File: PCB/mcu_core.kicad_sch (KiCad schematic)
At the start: 11 parts

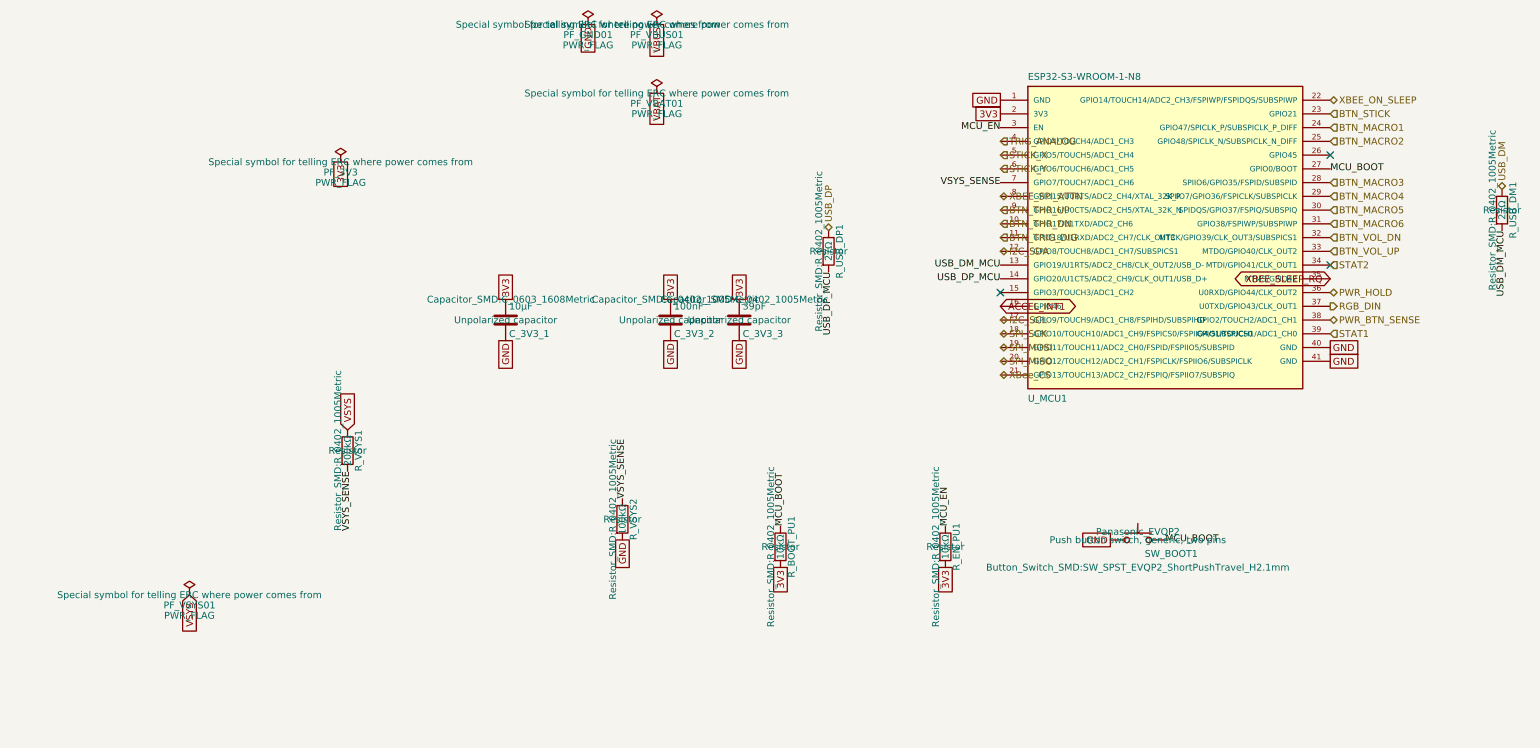
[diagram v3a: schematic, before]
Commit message: fix: make every BOM Value unambiguous for the fab, and switch D_INV_ISO1 to SOT-323 (#61)
* fix: make every BOM Value unambiguous for the fab, and switch D_INV_ISO1 to SOT-323

PCBWay flagged D_INV_ISO1: "BAT54W" is SOT-323 from nearly every maker, but we
had picked Yangjie's SOD-123 variant. A fab only sees Designator, Footprint,
Quantity and Value in the BOM (never MF/MPN/LCSC), so a bare part name is
ambiguous. Fixes the class of problem, not just this part:

- Every component's Value is now "<label> | <MPN> | <manufacturer> | <package>"
  (label dropped when it repeats the MPN; commas/periods stripped so the CSV
  never needs quoting). BT1 keeps its RIGHT-ANGLE HORIZONTAL note. Applied to
  all 81 parts across every sheet and the PCB.
- scripts/bom_values.py builds, applies, and checks these values, including
  that the PCB copy of Value/MF/MPN/footprint matches the schematic. New
  footprints must be added to its package table on purpose; hand-sourced parts
  with no MPN (J_STICK1) are listed explicitly.
- D_INV_ISO1 -> Diodes BAT54W-7-F in SOT-323 (common part, several makers).
  Pin 1 anode / pin 2 not connected / pin 3 cathode, confirmed against
  Nexperia's numbered pinning table and Diodes' datasheet. Uses KiCad's
  Diode:BAT54W symbol; PCB footprint replaced and rerouted. Electrically the
  same BAT54 family (30V, 200mA, 2uA leakage at 25V), so the SPICE model and
  scripts/spice/latch_sim.py still pass.
- Layout diagrams now say AO3401A for Q_PWR1 (they were stale since it was
  swapped from DMG2305UX) and BAT54W-7-F/SOT-323 for D_INV_ISO1.
- Repo CLAUDE.md documents the Value rule and the script.

ERC/DRC clean; production files regenerated.

Co-Authored-By: Claude Sonnet 5 <noreply@anthropic.com>

* chore: commit KiCad project settings (reordered used-designators list)

Co-Authored-By: Claude Sonnet 5 <noreply@anthropic.com>

---------

Co-authored-by: Claude Sonnet 5 <noreply@anthropic.com>
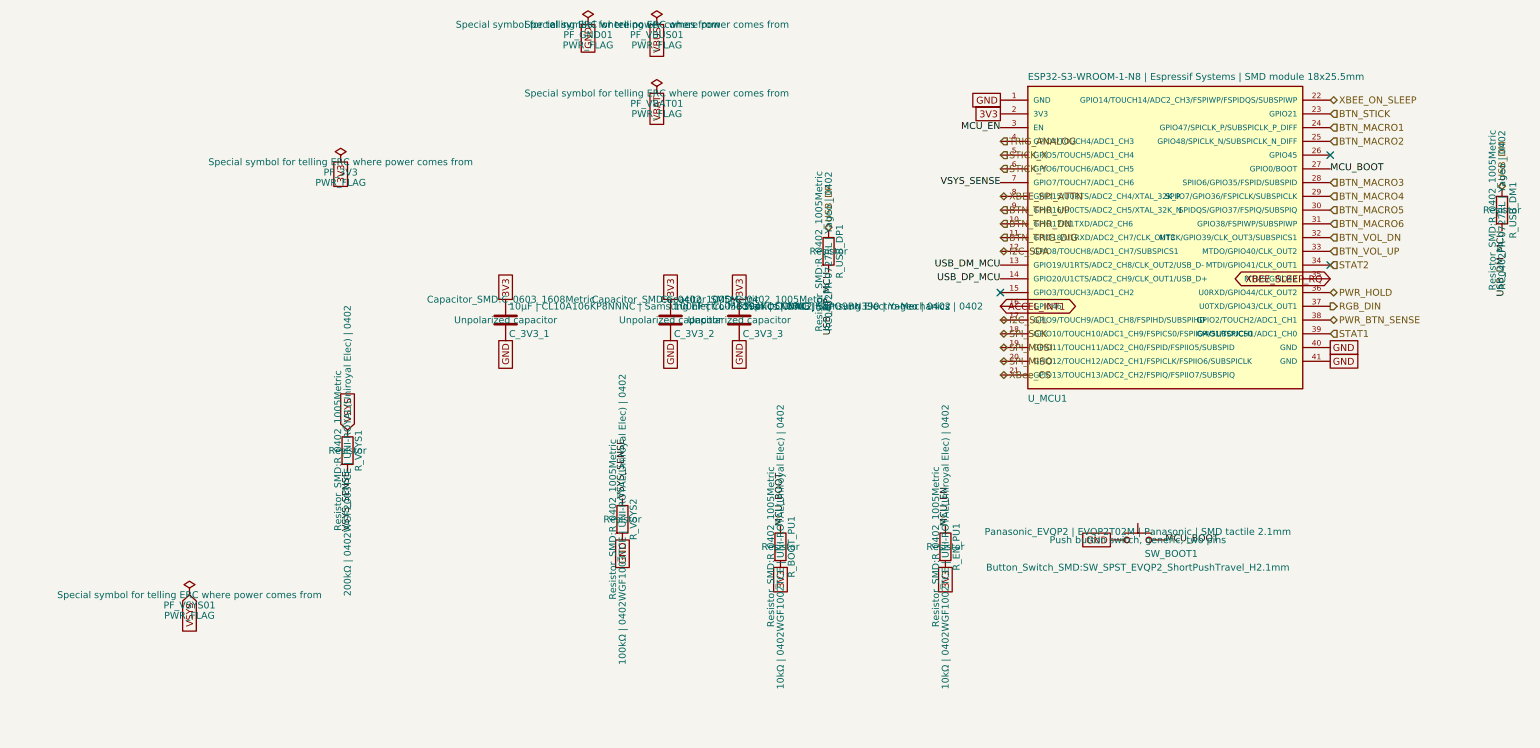
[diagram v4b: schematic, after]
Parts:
- C_3V3_1: value 10µF -> 10µF | CL10A106KP8NNNC | Samsung Electro-Mechanics | 0603
- C_3V3_2: value 100nF -> 100nF | CL05B104KO5NNNC | Samsung Electro-Mechanics | 0402
- C_3V3_3: value 39pF -> 39pF | CC0402JRNPO9BN390 | Yageo | 0402
- R_BOOT_PU1, R_EN_PU1: value 10kΩ -> 10kΩ | 0402WGF1002TCE | UNI-ROYAL(Uniroyal Elec) | 0402
- R_USB_DM1, R_USB_DP1: value 27Ω -> RC0402FR-0727RL | Yageo | 0402
- R_VSYS1: value 200kΩ -> 200kΩ | 0402WGF2003TCE | UNI-ROYAL(Uniroyal Elec) | 0402
- R_VSYS2: value 100kΩ -> 100kΩ | 0402WGF1003TCE | UNI-ROYAL(Uniroyal Elec) | 0402
- SW_BOOT1: value Panasonic_EVQP2 -> Panasonic_EVQP2 | EVQP2T02M | Panasonic | SMD tactile 2.1mm
- U_MCU1: value ESP32-S3-WROOM-1-N8 -> ESP32-S3-WROOM-1-N8 | Espressif Systems | SMD module 18x25.5mm
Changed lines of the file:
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@@
 			)
 		)
-		(property "Value" "10µF"
+		(property "Value" "10µF | CL10A106KP8NNNC | Samsung Electro-Mechanics | 0603"
 			(at 85.725 104.14 0)
 			(show_name no)
@@
 			)
 		)
-		(property "Value" "ESP32-S3-WROOM-1-N8"
+		(property "Value" "ESP32-S3-WROOM-1-N8 | Espressif Systems | SMD module 18x25.5mm"
 			(at 181.61 60.96 0)
 			(show_name no)
@@
 			)
 		)
-		(property "Value" "10kΩ"
+		(property "Value" "10kΩ | 0402WGF1002TCE | UNI-ROYAL(Uniroyal Elec) | 0402"
 			(at 135.89 148.59 90)
 			(show_name no)
@@
 			)
 		)
-		(property "Value" "39pF"
+		(property "Value" "39pF | CC0402JRNPO9BN390 | Yageo | 0402"
 			(at 128.905 104.14 0)
 			(show_name no)
@@
 			)
 		)
-		(property "Value" "10kΩ"
+		(property "Value" "10kΩ | 0402WGF1002TCE | UNI-ROYAL(Uniroyal Elec) | 0402"
 			(at 166.37 148.59 90)
 			(show_name no)
@@
 			)
 		)
-		(property "Value" "200kΩ"
+		(property "Value" "200kΩ | 0402WGF2003TCE | UNI-ROYAL(Uniroyal Elec) | 0402"
 			(at 55.88 130.81 90)
 			(show_name no)
@@
 			)
 		)
-		(property "Value" "Panasonic_EVQP2"
+		(property "Value" "Panasonic_EVQP2 | EVQP2T02M | Panasonic | SMD tactile 2.1mm"
 			(at 201.93 145.796 0)
 			(show_name no)
@@
 			)
 		)
-		(property "Value" "27Ω"
+		(property "Value" "RC0402FR-0727RL | Yageo | 0402"
 			(at 144.78 93.98 90)
 			(show_name no)
@@
 			)
 		)
-		(property "Value" "100kΩ"
+		(property "Value" "100kΩ | 0402WGF1003TCE | UNI-ROYAL(Uniroyal Elec) | 0402"
 			(at 106.68 143.51 90)
 			(show_name no)
@@
 			)
 		)
-		(property "Value" "100nF"
+		(property "Value" "100nF | CL05B104KO5NNNC | Samsung Electro-Mechanics | 0402"
 			(at 116.205 104.14 0)
 			(show_name no)
@@
 			)
 		)
-		(property "Value" "27Ω"
+		(property "Value" "RC0402FR-0727RL | Yageo | 0402"
 			(at 269.24 86.36 90)
 			(show_name no)
